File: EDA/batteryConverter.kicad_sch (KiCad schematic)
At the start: 10 parts, among them U9 TPS63000

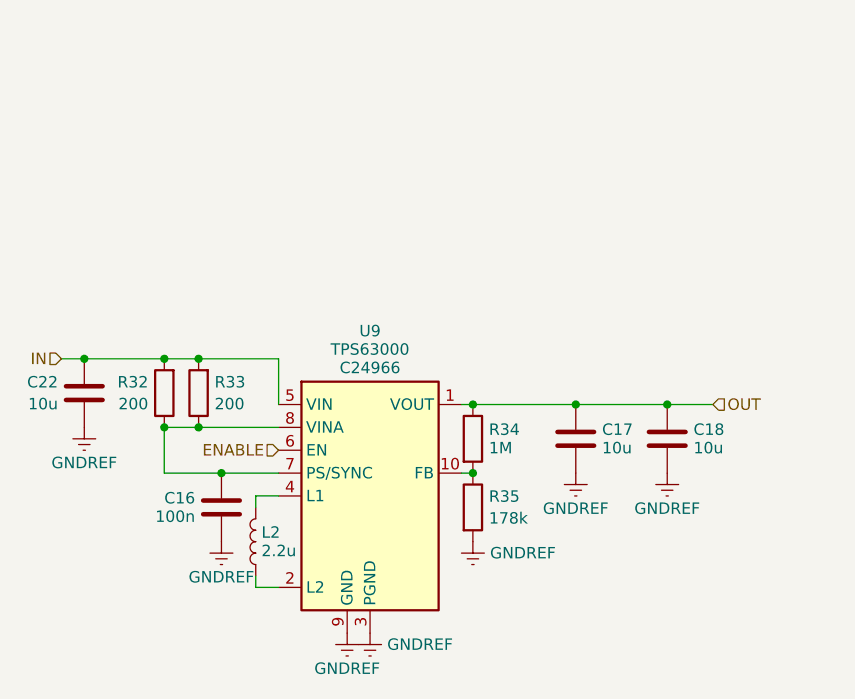
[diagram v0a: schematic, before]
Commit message: Add LDOs for battery and CAN power conditioning, add CD to SD card
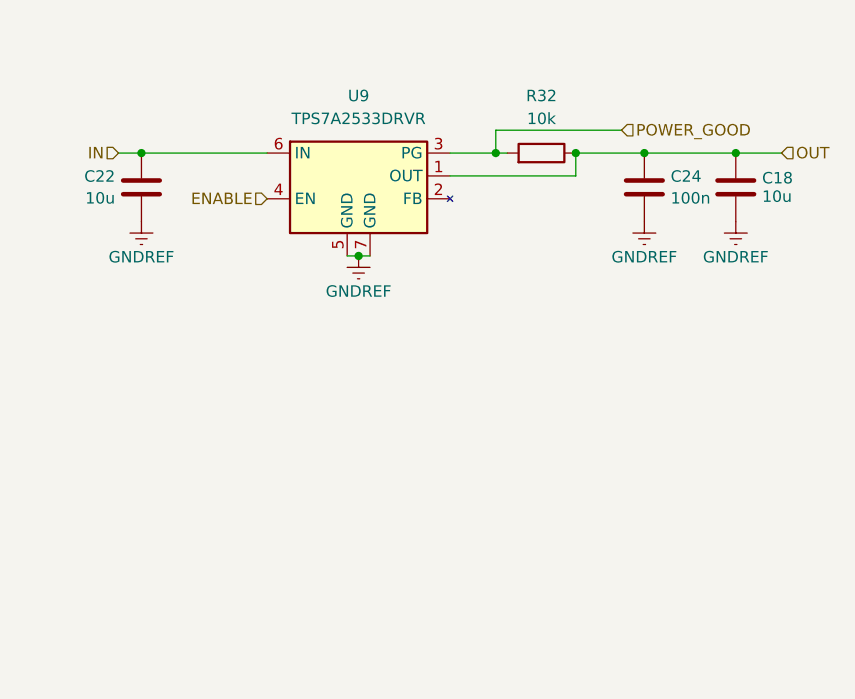
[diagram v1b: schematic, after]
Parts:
- removed C16: 100n, Capacitor_SMD:C_0603_1608Metric, symbol Library:C
- removed C17: 10u, Capacitor_SMD:C_0603_1608Metric, symbol Library:C
- removed L2: 2.2u, Library:L_4x4, symbol Library:L
- removed R33: 200, Resistor_SMD:R_0402_1005Metric, symbol Library:R
- removed R34: 1M, Resistor_SMD:R_0402_1005Metric, symbol Library:R
- removed R35: 178k, Resistor_SMD:R_0402_1005Metric, symbol Library:R
- removed U9: TPS63000, Package_SON:Texas_DRC0010J, symbol Library:TPS63001
- added C24: 100n, Capacitor_SMD:C_0603_1608Metric, symbol Library:C
- added U9: TPS7A2533DRVR, Package_SON:WSON-6-1EP_2x2mm_P0.65mm_EP1x1.6mm_ThermalVias, symbol Project:TPS7A2533DRVR
- R32: value 200 -> 10k; MPN C25087 -> C25744
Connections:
- net ENABLE: now also U9.4 (EN)
- net GNDREF: now also C24.2, U9.5 (GND), U9.7 (GND)
- net IN: now also U9.6 (IN); no longer R32.2
- net OUT: now also R32.1, C24.1, U9.1 (OUT)
- new net POWER_GOOD: R32.2, U9.3 (PG)

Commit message: Add 12v solenoid driver
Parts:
- C18, C22: MPN C19702 -> C96446
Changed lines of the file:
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@@
       (effects (font (size 1.27 1.27)) hide)
     )
-    (property "MPN" "C19702" (at 125.73 64.77 0)
+    (property "MPN" "C96446" (at 125.73 64.77 0)
       (effects (font (size 1.27 1.27)) hide)
     )
@@
       (effects (font (size 1.27 1.27)) hide)
     )
-    (property "MPN" "C19702" (at 191.77 64.77 0)
-      (effects (font (size 1.27 1.27)) hide)
-    )
+    (property "MPN" "C96446" (at 191.77 64.77 0)
+      (effects (font (size 1.27 1.27)) hide)
+    )

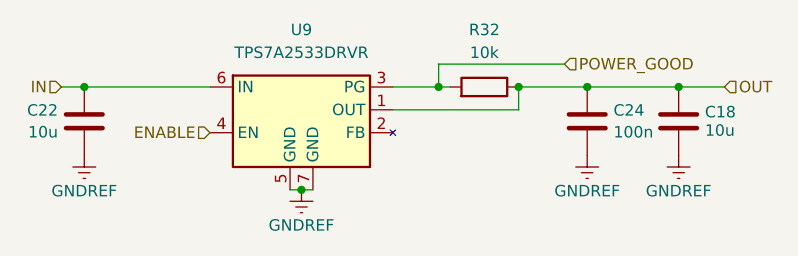
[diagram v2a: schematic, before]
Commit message: Renumber schematic
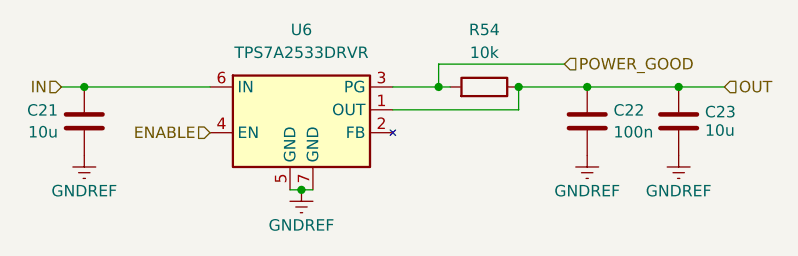
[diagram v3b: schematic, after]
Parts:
- renumbered C22 to C21, C24 to C22, C18 to C23, R32 to R54, U9 to U6
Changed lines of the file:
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@@
   (symbol (lib_id "Library:C") (at 125.73 64.77 0) (unit 1)
     (in_bom yes) (on_board yes) (dnp no) (fields_autoplaced)
-    (property "Reference" "C22" (at 122.809 63.5579 0)
+    (property "Reference" "C21" (at 122.809 63.5579 0)
       (effects (font (size 1.27 1.27)) (justify right))
     )
@@
       (project "DiveCAN Head2"
         (path "/ab021047-3849-453b-b3dc-d234ace3779d/113722a3-860b-4deb-adf7-14c4825bf494"
-          (reference "C22") (unit 1)
-        )
-        (path "/ab021047-3849-453b-b3dc-d234ace3779d/ef9e092e-8804-437c-bb6f-9d3759004dc2"
-          (reference "C22") (unit 1)
+          (reference "C21") (unit 1)
+        )
+        (path "/ab021047-3849-453b-b3dc-d234ace3779d/ef9e092e-8804-437c-bb6f-9d3759004dc2"
+          (reference "C10") (unit 1)
         )
       )
@@
   (symbol (lib_id "power:GNDREF") (at 149.86 72.39 0) (unit 1)
     (in_bom yes) (on_board yes) (dnp no) (fields_autoplaced)
-    (property "Reference" "#PWR0104" (at 149.86 78.74 0)
+    (property "Reference" "#PWR067" (at 149.86 78.74 0)
       (effects (font (size 1.27 1.27)) hide)
     )
@@
       (project "DiveCAN Head2"
         (path "/ab021047-3849-453b-b3dc-d234ace3779d/113722a3-860b-4deb-adf7-14c4825bf494"
-          (reference "#PWR0104") (unit 1)
-        )
-        (path "/ab021047-3849-453b-b3dc-d234ace3779d/ef9e092e-8804-437c-bb6f-9d3759004dc2"
-          (reference "#PWR054") (unit 1)
+          (reference "#PWR067") (unit 1)
+        )
+        (path "/ab021047-3849-453b-b3dc-d234ace3779d/ef9e092e-8804-437c-bb6f-9d3759004dc2"
+          (reference "#PWR049") (unit 1)
         )
       )
@@
   (symbol (lib_id "Library:R") (at 170.18 60.96 270) (mirror x) (unit 1)
     (in_bom yes) (on_board yes) (dnp no) (fields_autoplaced)
-    (property "Reference" "R32" (at 170.18 54.61 90)
+    (property "Reference" "R54" (at 170.18 54.61 90)
       (effects (font (size 1.27 1.27)))
     )
@@
       (project "DiveCAN Head2"
         (path "/ab021047-3849-453b-b3dc-d234ace3779d/113722a3-860b-4deb-adf7-14c4825bf494"
-          (reference "R32") (unit 1)
-        )
-        (path "/ab021047-3849-453b-b3dc-d234ace3779d/ef9e092e-8804-437c-bb6f-9d3759004dc2"
-          (reference "R32") (unit 1)
+          (reference "R54") (unit 1)
+        )
+        (path "/ab021047-3849-453b-b3dc-d234ace3779d/ef9e092e-8804-437c-bb6f-9d3759004dc2"
+          (reference "R41") (unit 1)
         )
       )
@@
   (symbol (lib_id "Project:TPS7A2533DRVR") (at 149.86 64.77 0) (unit 1)
     (in_bom yes) (on_board yes) (dnp no) (fields_autoplaced)
-    (property "Reference" "U9" (at 149.86 54.61 0)
+    (property "Reference" "U6" (at 149.86 54.61 0)
       (effects (font (size 1.27 1.27)))
     )
@@
       (project "DiveCAN Head2"
         (path "/ab021047-3849-453b-b3dc-d234ace3779d/ef9e092e-8804-437c-bb6f-9d3759004dc2"
-          (reference "U9") (unit 1)
-        )
-        (path "/ab021047-3849-453b-b3dc-d234ace3779d/113722a3-860b-4deb-adf7-14c4825bf494"
-          (reference "U9") (unit 1)
+          (reference "U6") (unit 1)
+        )
+        (path "/ab021047-3849-453b-b3dc-d234ace3779d/113722a3-860b-4deb-adf7-14c4825bf494"
+          (reference "U10") (unit 1)
         )
       )
@@
   (symbol (lib_id "power:GNDREF") (at 181.61 68.58 0) (unit 1)
     (in_bom yes) (on_board yes) (dnp no) (fields_autoplaced)
-    (property "Reference" "#PWR0103" (at 181.61 74.93 0)
+    (property "Reference" "#PWR068" (at 181.61 74.93 0)
       (effects (font (size 1.27 1.27)) hide)
     )
@@
       (project "DiveCAN Head2"
         (path "/ab021047-3849-453b-b3dc-d234ace3779d/113722a3-860b-4deb-adf7-14c4825bf494"
-          (reference "#PWR0103") (unit 1)
-        )
-        (path "/ab021047-3849-453b-b3dc-d234ace3779d/ef9e092e-8804-437c-bb6f-9d3759004dc2"
-          (reference "#PWR058") (unit 1)
+          (reference "#PWR068") (unit 1)
+        )
+        (path "/ab021047-3849-453b-b3dc-d234ace3779d/ef9e092e-8804-437c-bb6f-9d3759004dc2"
+          (reference "#PWR050") (unit 1)
         )
       )
@@
   (symbol (lib_id "power:GNDREF") (at 125.73 68.58 0) (unit 1)
     (in_bom yes) (on_board yes) (dnp no) (fields_autoplaced)
-    (property "Reference" "#PWR0101" (at 125.73 74.93 0)
+    (property "Reference" "#PWR066" (at 125.73 74.93 0)
       (effects (font (size 1.27 1.27)) hide)
     )
@@
       (project "DiveCAN Head2"
         (path "/ab021047-3849-453b-b3dc-d234ace3779d/113722a3-860b-4deb-adf7-14c4825bf494"
-          (reference "#PWR0101") (unit 1)
-        )
-        (path "/ab021047-3849-453b-b3dc-d234ace3779d/ef9e092e-8804-437c-bb6f-9d3759004dc2"
           (reference "#PWR066") (unit 1)
         )
+        (path "/ab021047-3849-453b-b3dc-d234ace3779d/ef9e092e-8804-437c-bb6f-9d3759004dc2"
+          (reference "#PWR048") (unit 1)
+        )
       )
     )
@@
   (symbol (lib_id "Library:C") (at 181.61 64.77 0) (unit 1)
     (in_bom yes) (on_board yes) (dnp no) (fields_autoplaced)
-    (property "Reference" "C24" (at 184.531 63.5579 0)
+    (property "Reference" "C22" (at 184.531 63.5579 0)
       (effects (font (size 1.27 1.27)) (justify left))
     )
@@
       (project "DiveCAN Head2"
         (path "/ab021047-3849-453b-b3dc-d234ace3779d/113722a3-860b-4deb-adf7-14c4825bf494"
-          (reference "C24") (unit 1)
-        )
-        (path "/ab021047-3849-453b-b3dc-d234ace3779d/ef9e092e-8804-437c-bb6f-9d3759004dc2"
-          (reference "C24") (unit 1)
+          (reference "C22") (unit 1)
+        )
+        (path "/ab021047-3849-453b-b3dc-d234ace3779d/ef9e092e-8804-437c-bb6f-9d3759004dc2"
+          (reference "C11") (unit 1)
         )
       )
@@
   (symbol (lib_id "power:GNDREF") (at 191.77 68.58 0) (unit 1)
     (in_bom yes) (on_board yes) (dnp no) (fields_autoplaced)
-    (property "Reference" "#PWR0102" (at 191.77 74.93 0)
+    (property "Reference" "#PWR069" (at 191.77 74.93 0)
       (effects (font (size 1.27 1.27)) hide)
     )
@@
       (project "DiveCAN Head2"
         (path "/ab021047-3849-453b-b3dc-d234ace3779d/113722a3-860b-4deb-adf7-14c4825bf494"
-          (reference "#PWR0102") (unit 1)
-        )
-        (path "/ab021047-3849-453b-b3dc-d234ace3779d/ef9e092e-8804-437c-bb6f-9d3759004dc2"
-          (reference "#PWR059") (unit 1)
+          (reference "#PWR069") (unit 1)
+        )
+        (path "/ab021047-3849-453b-b3dc-d234ace3779d/ef9e092e-8804-437c-bb6f-9d3759004dc2"
+          (reference "#PWR051") (unit 1)
         )
       )
@@
   (symbol (lib_id "Library:C") (at 191.77 64.77 0) (unit 1)
     (in_bom yes) (on_board yes) (dnp no) (fields_autoplaced)
-    (property "Reference" "C18" (at 194.691 63.746 0)
+    (property "Reference" "C23" (at 194.691 63.746 0)
       (effects (font (size 1.27 1.27)) (justify left))
     )
@@
       (project "DiveCAN Head2"
         (path "/ab021047-3849-453b-b3dc-d234ace3779d/113722a3-860b-4deb-adf7-14c4825bf494"
-          (reference "C18") (unit 1)
-        )
-        (path "/ab021047-3849-453b-b3dc-d234ace3779d/ef9e092e-8804-437c-bb6f-9d3759004dc2"
-          (reference "C18") (unit 1)
-        )
-      )
+          (reference "C23") (unit 1)
+        )
+        (path "/ab021047-3849-453b-b3dc-d234ace3779d/ef9e092e-8804-437c-bb6f-9d3759004dc2"
+          (reference "C12") (unit 1)
+        )
+      )

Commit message: Move power logic into power distribution sheet
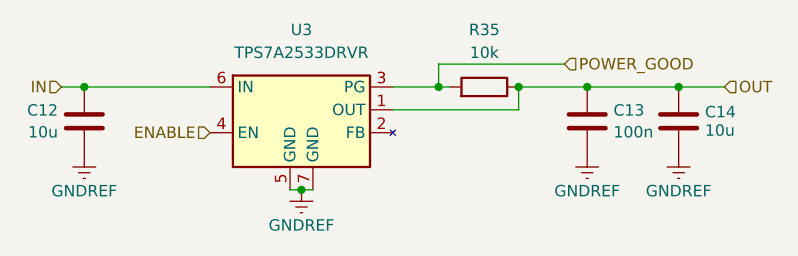
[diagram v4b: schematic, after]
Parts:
- renumbered C21 to C12, C22 to C13, C23 to C14, R54 to R35, U6 to U3

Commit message: Add input protection to the power distribution
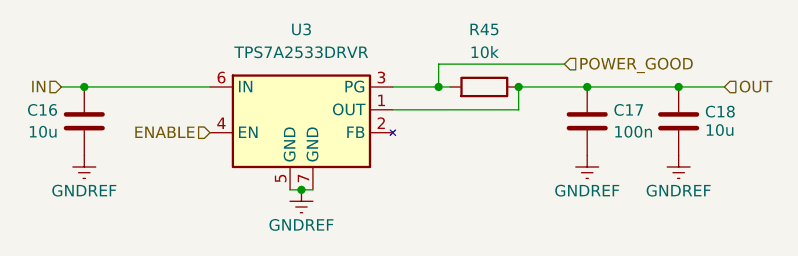
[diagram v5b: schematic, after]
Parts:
- renumbered C12 to C16, C13 to C17, C14 to C18, R35 to R45
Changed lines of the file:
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@@
   (symbol (lib_id "Library:C") (at 125.73 64.77 0) (unit 1)
     (in_bom yes) (on_board yes) (dnp no) (fields_autoplaced)
-    (property "Reference" "C12" (at 122.809 63.5579 0)
+    (property "Reference" "C16" (at 122.809 63.5579 0)
       (effects (font (size 1.27 1.27)) (justify right))
     )
@@
       (project "DiveCAN Head2"
         (path "/ab021047-3849-453b-b3dc-d234ace3779d/a695df33-b48d-4ed9-a29f-bb0896c20222/15c577d2-26ea-416d-a101-a0b8b72da3d4"
-          (reference "C12") (unit 1)
-        )
-        (path "/ab021047-3849-453b-b3dc-d234ace3779d/a695df33-b48d-4ed9-a29f-bb0896c20222/a167d0ec-77af-4b56-93ce-66f247a312ee"
-          (reference "C9") (unit 1)
+          (reference "C16") (unit 1)
+        )
+        (path "/ab021047-3849-453b-b3dc-d234ace3779d/a695df33-b48d-4ed9-a29f-bb0896c20222/a167d0ec-77af-4b56-93ce-66f247a312ee"
+          (reference "C13") (unit 1)
         )
       )
@@
   (symbol (lib_id "power:GNDREF") (at 149.86 72.39 0) (unit 1)
     (in_bom yes) (on_board yes) (dnp no) (fields_autoplaced)
-    (property "Reference" "#PWR041" (at 149.86 78.74 0)
+    (property "Reference" "#PWR045" (at 149.86 78.74 0)
       (effects (font (size 1.27 1.27)) hide)
     )
@@
       (project "DiveCAN Head2"
         (path "/ab021047-3849-453b-b3dc-d234ace3779d/a695df33-b48d-4ed9-a29f-bb0896c20222/a167d0ec-77af-4b56-93ce-66f247a312ee"
-          (reference "#PWR041") (unit 1)
-        )
-        (path "/ab021047-3849-453b-b3dc-d234ace3779d/a695df33-b48d-4ed9-a29f-bb0896c20222/15c577d2-26ea-416d-a101-a0b8b72da3d4"
           (reference "#PWR045") (unit 1)
         )
+        (path "/ab021047-3849-453b-b3dc-d234ace3779d/a695df33-b48d-4ed9-a29f-bb0896c20222/15c577d2-26ea-416d-a101-a0b8b72da3d4"
+          (reference "#PWR049") (unit 1)
+        )
       )
     )
@@
   (symbol (lib_id "Library:R") (at 170.18 60.96 270) (mirror x) (unit 1)
     (in_bom yes) (on_board yes) (dnp no) (fields_autoplaced)
-    (property "Reference" "R35" (at 170.18 54.61 90)
+    (property "Reference" "R45" (at 170.18 54.61 90)
       (effects (font (size 1.27 1.27)))
     )
@@
       (project "DiveCAN Head2"
         (path "/ab021047-3849-453b-b3dc-d234ace3779d/a695df33-b48d-4ed9-a29f-bb0896c20222/15c577d2-26ea-416d-a101-a0b8b72da3d4"
-          (reference "R35") (unit 1)
-        )
-        (path "/ab021047-3849-453b-b3dc-d234ace3779d/a695df33-b48d-4ed9-a29f-bb0896c20222/a167d0ec-77af-4b56-93ce-66f247a312ee"
-          (reference "R34") (unit 1)
+          (reference "R45") (unit 1)
+        )
+        (path "/ab021047-3849-453b-b3dc-d234ace3779d/a695df33-b48d-4ed9-a29f-bb0896c20222/a167d0ec-77af-4b56-93ce-66f247a312ee"
+          (reference "R44") (unit 1)
         )
       )
@@
   (symbol (lib_id "power:GNDREF") (at 181.61 68.58 0) (unit 1)
     (in_bom yes) (on_board yes) (dnp no) (fields_autoplaced)
-    (property "Reference" "#PWR042" (at 181.61 74.93 0)
+    (property "Reference" "#PWR046" (at 181.61 74.93 0)
       (effects (font (size 1.27 1.27)) hide)
     )
@@
       (project "DiveCAN Head2"
         (path "/ab021047-3849-453b-b3dc-d234ace3779d/a695df33-b48d-4ed9-a29f-bb0896c20222/a167d0ec-77af-4b56-93ce-66f247a312ee"
-          (reference "#PWR042") (unit 1)
-        )
-        (path "/ab021047-3849-453b-b3dc-d234ace3779d/a695df33-b48d-4ed9-a29f-bb0896c20222/15c577d2-26ea-416d-a101-a0b8b72da3d4"
           (reference "#PWR046") (unit 1)
         )
+        (path "/ab021047-3849-453b-b3dc-d234ace3779d/a695df33-b48d-4ed9-a29f-bb0896c20222/15c577d2-26ea-416d-a101-a0b8b72da3d4"
+          (reference "#PWR050") (unit 1)
+        )
       )
     )
@@
   (symbol (lib_id "power:GNDREF") (at 125.73 68.58 0) (unit 1)
     (in_bom yes) (on_board yes) (dnp no) (fields_autoplaced)
-    (property "Reference" "#PWR040" (at 125.73 74.93 0)
+    (property "Reference" "#PWR044" (at 125.73 74.93 0)
       (effects (font (size 1.27 1.27)) hide)
     )
@@
       (project "DiveCAN Head2"
         (path "/ab021047-3849-453b-b3dc-d234ace3779d/a695df33-b48d-4ed9-a29f-bb0896c20222/a167d0ec-77af-4b56-93ce-66f247a312ee"
-          (reference "#PWR040") (unit 1)
-        )
-        (path "/ab021047-3849-453b-b3dc-d234ace3779d/a695df33-b48d-4ed9-a29f-bb0896c20222/15c577d2-26ea-416d-a101-a0b8b72da3d4"
           (reference "#PWR044") (unit 1)
         )
+        (path "/ab021047-3849-453b-b3dc-d234ace3779d/a695df33-b48d-4ed9-a29f-bb0896c20222/15c577d2-26ea-416d-a101-a0b8b72da3d4"
+          (reference "#PWR048") (unit 1)
+        )
       )
     )
@@
   (symbol (lib_id "Library:C") (at 181.61 64.77 0) (unit 1)
     (in_bom yes) (on_board yes) (dnp no) (fields_autoplaced)
-    (property "Reference" "C13" (at 184.531 63.5579 0)
+    (property "Reference" "C17" (at 184.531 63.5579 0)
       (effects (font (size 1.27 1.27)) (justify left))
     )
@@
       (project "DiveCAN Head2"
         (path "/ab021047-3849-453b-b3dc-d234ace3779d/a695df33-b48d-4ed9-a29f-bb0896c20222/15c577d2-26ea-416d-a101-a0b8b72da3d4"
-          (reference "C13") (unit 1)
-        )
-        (path "/ab021047-3849-453b-b3dc-d234ace3779d/a695df33-b48d-4ed9-a29f-bb0896c20222/a167d0ec-77af-4b56-93ce-66f247a312ee"
-          (reference "C10") (unit 1)
+          (reference "C17") (unit 1)
+        )
+        (path "/ab021047-3849-453b-b3dc-d234ace3779d/a695df33-b48d-4ed9-a29f-bb0896c20222/a167d0ec-77af-4b56-93ce-66f247a312ee"
+          (reference "C14") (unit 1)
         )
       )
@@
   (symbol (lib_id "power:GNDREF") (at 191.77 68.58 0) (unit 1)
     (in_bom yes) (on_board yes) (dnp no) (fields_autoplaced)
-    (property "Reference" "#PWR043" (at 191.77 74.93 0)
+    (property "Reference" "#PWR047" (at 191.77 74.93 0)
       (effects (font (size 1.27 1.27)) hide)
     )
@@
       (project "DiveCAN Head2"
         (path "/ab021047-3849-453b-b3dc-d234ace3779d/a695df33-b48d-4ed9-a29f-bb0896c20222/a167d0ec-77af-4b56-93ce-66f247a312ee"
-          (reference "#PWR043") (unit 1)
-        )
-        (path "/ab021047-3849-453b-b3dc-d234ace3779d/a695df33-b48d-4ed9-a29f-bb0896c20222/15c577d2-26ea-416d-a101-a0b8b72da3d4"
           (reference "#PWR047") (unit 1)
         )
+        (path "/ab021047-3849-453b-b3dc-d234ace3779d/a695df33-b48d-4ed9-a29f-bb0896c20222/15c577d2-26ea-416d-a101-a0b8b72da3d4"
+          (reference "#PWR051") (unit 1)
+        )
       )
     )
@@
   (symbol (lib_id "Library:C") (at 191.77 64.77 0) (unit 1)
     (in_bom yes) (on_board yes) (dnp no) (fields_autoplaced)
-    (property "Reference" "C14" (at 194.691 63.746 0)
+    (property "Reference" "C18" (at 194.691 63.746 0)
       (effects (font (size 1.27 1.27)) (justify left))
     )
@@
       (project "DiveCAN Head2"
         (path "/ab021047-3849-453b-b3dc-d234ace3779d/a695df33-b48d-4ed9-a29f-bb0896c20222/15c577d2-26ea-416d-a101-a0b8b72da3d4"
-          (reference "C14") (unit 1)
-        )
-        (path "/ab021047-3849-453b-b3dc-d234ace3779d/a695df33-b48d-4ed9-a29f-bb0896c20222/a167d0ec-77af-4b56-93ce-66f247a312ee"
-          (reference "C11") (unit 1)
-        )
-      )
+          (reference "C18") (unit 1)
+        )
+        (path "/ab021047-3849-453b-b3dc-d234ace3779d/a695df33-b48d-4ed9-a29f-bb0896c20222/a167d0ec-77af-4b56-93ce-66f247a312ee"
+          (reference "C15") (unit 1)
+        )
+      )

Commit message: Rev 2.2 fabrication tweaks
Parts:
- U3: JlcRotOffset (none) -> 0; MPN (none) -> C2867820
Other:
- note added: "340mV dropout voltage at full load"
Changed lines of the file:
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@@
     (stroke (width 0) (type default))
+  )
+  (text "340mV dropout voltage at full load" (at 156.21 48.26 0)
+    (effects (font (size 1.27 1.27)) (justify left bottom))
   )
   (hierarchical_label "ENABLE" (shape input) (at 139.7 66.04 180) (fields_autoplaced)
@@
       (effects (font (size 1.27 1.27)) hide)
     )
+    (property "MPN" "C2867820" (at 149.86 64.77 0)
+      (effects (font (size 1.27 1.27)) hide)
+    )
+    (property "JlcRotOffset" "0" (at 149.86 64.77 0)
+      (effects (font (size 1.27 1.27)) hide)
+    )
